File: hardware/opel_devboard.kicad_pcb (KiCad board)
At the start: 2 copper layers, 35 parts, among them P1 CONN_01X16, P2 CONN_01X06, P4 CONN_01X04, P5 CONN_01X04, SW1 SPST, SW2 SPST, U1 ISO1050, U2 LPC11C14, U3 MCP2515_TSSOP, U4 ISO1050, U5 MCP1755

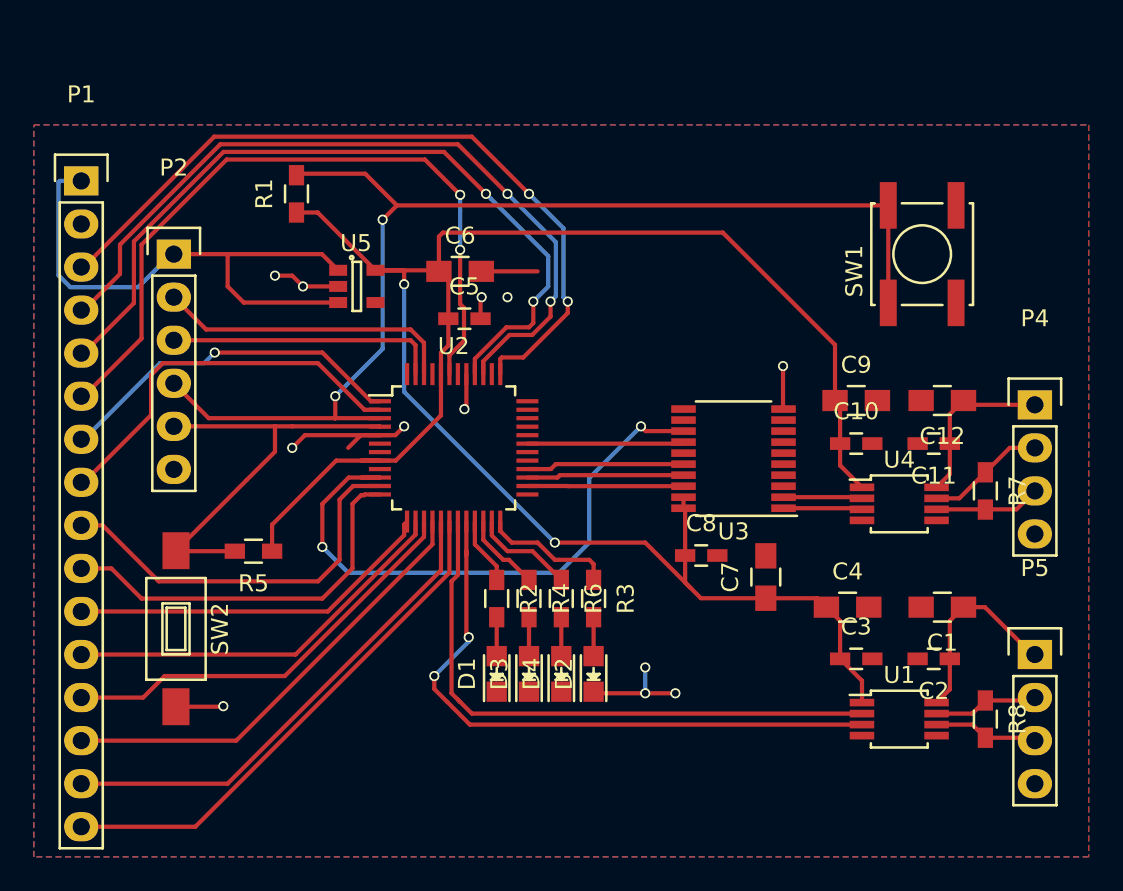
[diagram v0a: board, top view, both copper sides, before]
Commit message: updadted pinout and buttons
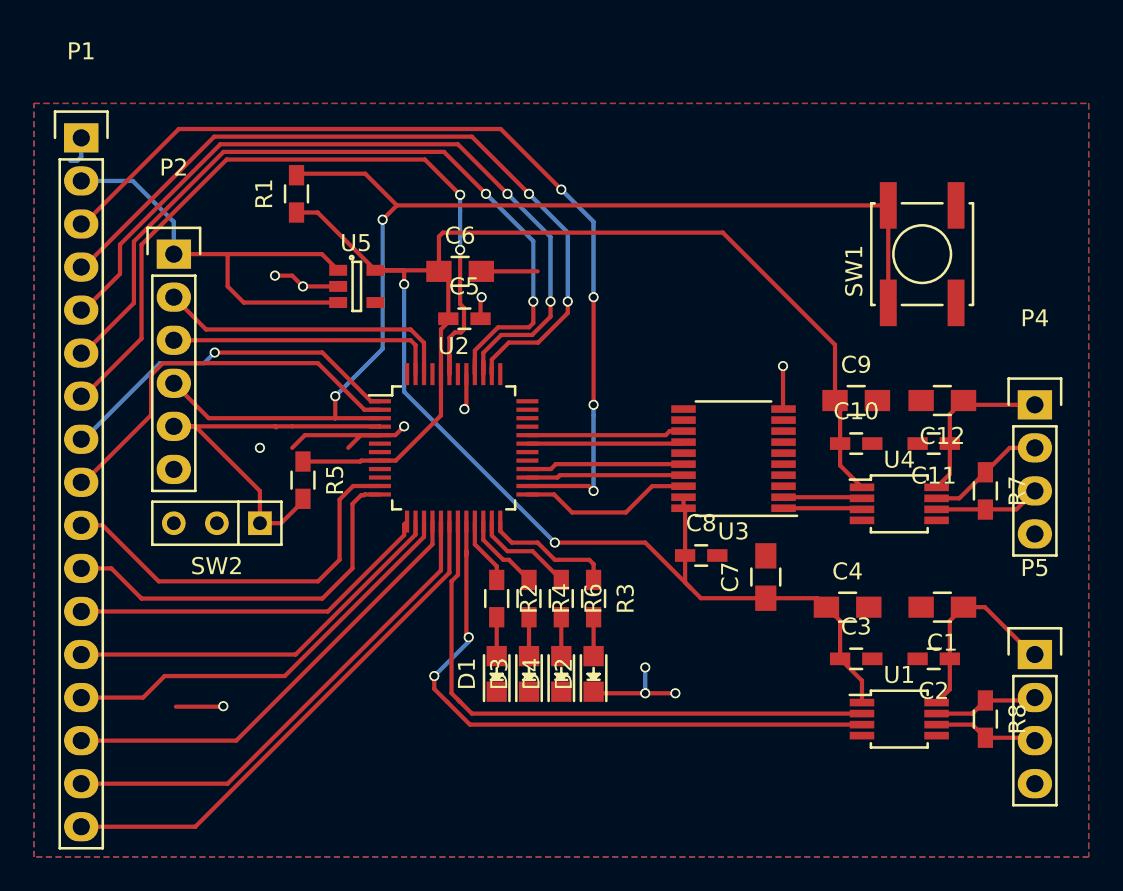
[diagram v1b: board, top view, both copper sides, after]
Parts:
- P1: value CONN_01X16 -> CONN_01X17; footprint Pin_Headers:Pin_Header_Straight_1x16 -> Pin_Headers:Pin_Header_Straight_1x17
- SW2: footprint Buttons_Switches_SMD:SW_SPST_FSMSM -> Buttons_Switches_ThroughHole:SW_Micro_SPST
- moved SW2 6.67 mm to (164.5, 71.8), turned to 180 degrees
- moved R5 5.11 mm to (169.5, 69.2), turned to 270 degrees
- moved P1 2.54 mm to (156.5, 49.0)
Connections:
- P1 pad 1: +5V -> GND
- P1 pad 10: /Micro Controller/PIO2_8 -> /Micro Controller/PIO2_7
- P1 pad 11: /Micro Controller/PIO2_1 -> /Micro Controller/PIO2_8
- P1 pad 12: /Micro Controller/PIO0_3 -> /Micro Controller/PIO2_1
- P1 pad 13: /Micro Controller/PIO0_4 -> /Micro Controller/PIO0_3
- P1 pad 14: /Micro Controller/PIO0_5 -> /Micro Controller/PIO0_4
- P1 pad 15: /Micro Controller/PIO1_9 -> /Micro Controller/PIO0_5
- P1 pad 16: /Micro Controller/PIO2_4 -> /Micro Controller/PIO1_9
- P1 pad 2: GND -> +5V
- P1 pad 3: /Micro Controller/PIO3_1 -> /Micro Controller/PIO2_2
- P1 pad 4: /Micro Controller/PIO1_3 -> /Micro Controller/PIO2_3
- P1 pad 5: /Micro Controller/PIO1_4 -> /Micro Controller/PIO1_3
- P1 pad 6: /Micro Controller/PIO3_2 -> /Micro Controller/PIO1_4
- P1 pad 7: /Micro Controller/PIO2_6 -> /Micro Controller/PIO3_2
- P1 pad 8: /Micro Controller/PIO0_1 -> /Micro Controller/PIO2_6
- P1 pad 9: /Micro Controller/PIO2_7 -> /Micro Controller/PIO0_1
- U2 pad 25: /Micro Controller/PIO2_10 -> Net-(U2-Pad25)
- U2 pad 26: Net-(U2-Pad26) -> /Micro Controller/PIO2_2
- U2 pad 38: Net-(U2-Pad38) -> /Micro Controller/PIO2_3
- U3 pad 13: Net-(U2-Pad10) -> /Micro Controller/PIO0_11
- U3 pad 18: Net-(U2-Pad26) -> Net-(U2-Pad25)
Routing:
- net /Micro Controller/PIO2_2: track 0.00 -> 54.7 mm, vias 0 -> 4
- net /Micro Controller/PIO2_3: track 0.00 -> 45.9 mm, vias 0 -> 2
- net /Micro Controller/PIO3_1: track 45.0 -> 0.00 mm, vias 2 -> 0
- net Net-(U2-Pad10): track 35.5 -> 0.00 mm, vias 2 -> 0
- net Net-(U2-Pad25): track 0.00 -> 10.3 mm
- net /Micro Controller/PIO0_11: track 0.00 -> 9.31 mm
- net Net-(U2-Pad26): track 9.21 -> 0.00 mm
- net +5V: track 33.7 -> 27.4 mm
- net +3V3: track 122.7 -> 116.6 mm
- net (no net): track 0.00 -> 2.81 mm, vias 1 -> 2
- net /Micro Controller/PIO3_2: track 43.3 -> 44.6 mm
- net /Input Connectors/MCU_PROG_N: track 25.4 -> 24.2 mm
- net GND: track 31.8 -> 30.8 mm, vias 11 -> 9
- net /Micro Controller/PIO1_3: track 45.8 -> 46.6 mm

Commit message: panelized
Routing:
- net (no net): track 2.81 -> 0.00 mm, vias 2 -> 1
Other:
- board text added: "+5"
- board text added: "CAN1"
- board text added: "CAN2"
- board text added: "GND"
- board text added: "ISP"
- board text added: "MIT LPC11C DEV"
- board text added: "RESET"
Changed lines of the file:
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@@
   (general
     (links 103)
-    (no_connects 1)
-    (area 0 0 0 0)
+    (no_connects 0)
+    (area 151.355667 42.797 217.833334 91.647001)
     (thickness 1.6)
-    (drawings 0)
-    (tracks 358)
+    (drawings 7)
+    (tracks 355)
     (zones 0)
     (modules 35)
@@
   (layers
     (0 F.Cu signal)
-    (31 B.Cu signal hide)
+    (31 B.Cu signal)
     (32 B.Adhes user)
     (33 F.Adhes user)
@@
     (aux_axis_origin 0 0)
     (grid_origin 212.344 29.845)
-    (visible_elements FFFFFF7F)
+    (visible_elements FFFEFF7F)
     (pcbplotparams
       (layerselection 0x00030_80000001)
@@
     (descr "Through hole pin header")
     (tags "pin header")
-    (fp_text reference P2 (at 0 -5.1) (layer F.SilkS)
+    (fp_text reference P2 (at 0 -2.54) (layer F.SilkS)
       (effects (font (size 1 1) (thickness 0.15)))
     )
@@
     (tags "capacitor 0805")
     (attr smd)
-    (fp_text reference C1 (at 0 -2.1 180) (layer F.SilkS)
+    (fp_text reference C1 (at 0 2.413 180) (layer F.SilkS)
       (effects (font (size 1 1) (thickness 0.15)))
     )
@@
     (tags "capacitor 0603")
     (attr smd)
-    (fp_text reference C2 (at 0 -1.9 180) (layer F.SilkS)
+    (fp_text reference C2 (at -3.048 -0.254 180) (layer F.SilkS)
       (effects (font (size 1 1) (thickness 0.15)))
     )
@@
     (tags "capacitor 0603")
     (attr smd)
-    (fp_text reference C3 (at 0 -1.9) (layer F.SilkS)
+    (fp_text reference C3 (at -3.175 0.254) (layer F.SilkS)
       (effects (font (size 1 1) (thickness 0.15)))
     )
@@
     (tags "capacitor 0805")
     (attr smd)
-    (fp_text reference C4 (at 0 -2.1) (layer F.SilkS)
+    (fp_text reference C4 (at 0 -2.413) (layer F.SilkS)
       (effects (font (size 1 1) (thickness 0.15)))
     )
@@
     (tags "capacitor 0603")
     (attr smd)
-    (fp_text reference C5 (at 0 -1.9) (layer F.SilkS)
+    (fp_text reference C5 (at 3.429 0) (layer F.SilkS)
       (effects (font (size 1 1) (thickness 0.15)))
     )
@@
     (tags "capacitor 0805")
     (attr smd)
-    (fp_text reference C6 (at 0 -2.1) (layer F.SilkS)
+    (fp_text reference C6 (at 3.683 0.254) (layer F.SilkS)
       (effects (font (size 1 1) (thickness 0.15)))
     )
@@
     (tags "capacitor 0805")
     (attr smd)
-    (fp_text reference C7 (at 0 -2.1 90) (layer F.SilkS)
+    (fp_text reference C7 (at -3.175 -0.381 180) (layer F.SilkS)
       (effects (font (size 1 1) (thickness 0.15)))
     )
@@
     (tags "capacitor 0603")
     (attr smd)
-    (fp_text reference C8 (at 0 -1.9) (layer F.SilkS)
+    (fp_text reference C8 (at 0 1.905) (layer F.SilkS)
       (effects (font (size 1 1) (thickness 0.15)))
     )
@@
     (tags "capacitor 0805")
     (attr smd)
-    (fp_text reference C9 (at 0 -2.1) (layer F.SilkS)
+    (fp_text reference C9 (at 0 -1.651) (layer F.SilkS)
       (effects (font (size 1 1) (thickness 0.15)))
     )
@@
     (tags "capacitor 0603")
     (attr smd)
-    (fp_text reference C10 (at 0 -1.9) (layer F.SilkS)
+    (fp_text reference C10 (at -1.905 2.159 90) (layer F.SilkS)
       (effects (font (size 1 1) (thickness 0.15)))
     )
@@
     (tags "capacitor 0603")
     (attr smd)
-    (fp_text reference C11 (at 0 -1.9 180) (layer F.SilkS)
+    (fp_text reference C11 (at -3.048 0.381 180) (layer F.SilkS)
       (effects (font (size 1 1) (thickness 0.15)))
     )
@@
     (tags "capacitor 0805")
     (attr smd)
-    (fp_text reference C12 (at 0 -2.1 180) (layer F.SilkS)
+    (fp_text reference C12 (at 0 1.651 180) (layer F.SilkS)
       (effects (font (size 1 1) (thickness 0.15)))
     )
@@
     (tags "LED 0805 SMD")
     (attr smd)
-    (fp_text reference D1 (at 0 -1.75 90) (layer F.SilkS)
+    (fp_text reference D1 (at 0 -2.921 90) (layer F.SilkS)
       (effects (font (size 1 1) (thickness 0.15)))
     )
@@
     (tags "LED 0805 SMD")
     (attr smd)
-    (fp_text reference D2 (at 0 -1.75 90) (layer F.SilkS)
+    (fp_text reference D2 (at 0 2.794 90) (layer F.SilkS)
       (effects (font (size 1 1) (thickness 0.15)))
     )
@@
     (tags "LED 0805 SMD")
     (attr smd)
-    (fp_text reference D3 (at 0 -1.75 90) (layer F.SilkS)
+    (fp_text reference D3 (at 0 -3.556 90) (layer F.SilkS)
       (effects (font (size 1 1) (thickness 0.15)))
     )
@@
     (tags "LED 0805 SMD")
     (attr smd)
-    (fp_text reference D4 (at 0 -1.75 90) (layer F.SilkS)
+    (fp_text reference D4 (at 0 3.429 90) (layer F.SilkS)
       (effects (font (size 1 1) (thickness 0.15)))
     )
@@
     (descr "Through hole pin header")
     (tags "pin header")
-    (fp_text reference P4 (at 0 -5.1) (layer F.SilkS)
+    (fp_text reference P4 (at 0 -2.54) (layer F.SilkS)
       (effects (font (size 1 1) (thickness 0.15)))
     )
@@
     (descr "Through hole pin header")
     (tags "pin header")
-    (fp_text reference P5 (at 0 -5.1) (layer F.SilkS)
+    (fp_text reference P5 (at 0 -2.667) (layer F.SilkS)
       (effects (font (size 1 1) (thickness 0.15)))
     )
@@
     (tags "resistor 0603")
     (attr smd)
-    (fp_text reference R1 (at 0 -1.9 90) (layer F.SilkS)
+    (fp_text reference R1 (at 3.429 0 180) (layer F.SilkS)
       (effects (font (size 1 1) (thickness 0.15)))
     )
@@
     (tags "resistor 0603")
     (attr smd)
-    (fp_text reference R2 (at 0 -1.9 270) (layer F.SilkS)
+    (fp_text reference R2 (at 0 2.921 270) (layer F.SilkS)
       (effects (font (size 1 1) (thickness 0.15)))
     )
@@
     (tags "resistor 0603")
     (attr smd)
-    (fp_text reference R3 (at 0 -1.9 270) (layer F.SilkS)
+    (fp_text reference R3 (at 0 -2.794 270) (layer F.SilkS)
       (effects (font (size 1 1) (thickness 0.15)))
     )
@@
     (tags "resistor 0603")
     (attr smd)
-    (fp_text reference R4 (at 0 -1.9 270) (layer F.SilkS)
+    (fp_text reference R4 (at 0 3.556 270) (layer F.SilkS)
       (effects (font (size 1 1) (thickness 0.15)))
     )
@@
     (tags "resistor 0603")
     (attr smd)
-    (fp_text reference R5 (at 0 -1.9 270) (layer F.SilkS)
+    (fp_text reference R5 (at -3.175 0.381 360) (layer F.SilkS)
       (effects (font (size 1 1) (thickness 0.15)))
     )
@@
     (tags "resistor 0603")
     (attr smd)
-    (fp_text reference R6 (at 0 -1.9 270) (layer F.SilkS)
+    (fp_text reference R6 (at 0 -3.429 270) (layer F.SilkS)
       (effects (font (size 1 1) (thickness 0.15)))
     )
@@
     (tags "resistor 0603")
     (attr smd)
-    (fp_text reference R7 (at 0 -1.9 270) (layer F.SilkS)
+    (fp_text reference R7 (at 3.175 0 270) (layer F.SilkS)
       (effects (font (size 1 1) (thickness 0.15)))
     )
@@
     (tags "resistor 0603")
     (attr smd)
-    (fp_text reference R8 (at 0 -1.9 270) (layer F.SilkS)
+    (fp_text reference R8 (at 3.683 0 360) (layer F.SilkS)
       (effects (font (size 1 1) (thickness 0.15)))
     )
@@
     (tags "SSOP 0.65")
     (attr smd)
-    (fp_text reference U1 (at 0 -2.6) (layer F.SilkS)
+    (fp_text reference U1 (at 0 3.048) (layer F.SilkS)
       (effects (font (size 1 1) (thickness 0.15)))
     )
@@
     (tags "SSOP 0.65")
     (attr smd)
-    (fp_text reference U3 (at 0 -4.3 180) (layer F.SilkS)
+    (fp_text reference U3 (at 0 4.445 180) (layer F.SilkS)
       (effects (font (size 1 1) (thickness 0.15)))
     )
@@
     (tags "SSOP 0.65")
     (attr smd)
-    (fp_text reference U4 (at 0 -2.6) (layer F.SilkS)
+    (fp_text reference U4 (at 0 2.413) (layer F.SilkS)
       (effects (font (size 1 1) (thickness 0.15)))
     )
@@
     (descr "Through hole pin header")
     (tags "pin header")
-    (fp_text reference P1 (at 0 -5.1) (layer F.SilkS)
+    (fp_text reference P1 (at 3.175 40.513) (layer F.SilkS)
       (effects (font (size 1 1) (thickness 0.15)))
     )
@@
     )
   )
-  (segment (start 162.04968 82.58043) (end 164.81557 82.58043) (width 0.25) (layer F.Cu) (net 0))
-  (segment (start 164.81557 82.58043) (end 164.846 82.55) (width 0.25) (layer F.Cu) (net 0))
-  (via (at 164.846 82.55) (size 0.6) (drill 0.4) (layers F.Cu B.Cu) (net 0))
+  (gr_text "MIT LPC11C DEV\n" (at 186.944 86.36) (layer F.SilkS)
+    (effects (font (size 1.5 1.5) (thickness 0.3)))
+  )
+  (gr_text CAN2 (at 212.344 57.785 270) (layer F.SilkS)
+    (effects (font (size 1.5 1.5) (thickness 0.3)))
+  )
+  (gr_text "CAN1\n" (at 207.264 88.9) (layer F.SilkS)
+    (effects (font (size 1.5 1.5) (thickness 0.3)))
+  )
+  (gr_text ISP (at 164.084 76.835) (layer F.SilkS)
+    (effects (font (size 1.5 1.5) (thickness 0.3)))
+  )
+  (gr_text RESET (at 205.994 49.53) (layer F.SilkS)
+    (effects (font (size 1.5 1.5) (thickness 0.3)))
+  )
+  (gr_text +5 (at 160.909 51.435) (layer F.SilkS)
+    (effects (font (size 1.5 1.5) (thickness 0.3)))
+  )
+  (gr_text GND (at 161.544 48.895) (layer F.SilkS)
+    (effects (font (size 1.5 1.5) (thickness 0.3)))
+  )
   (via (at 167.005 67.31) (size 0.6) (drill 0.4) (layers F.Cu B.Cu) (net 0))
   (segment (start 180.02 59.69) (end 180.02 58.486) (width 0.25) (layer F.Cu) (net 1))

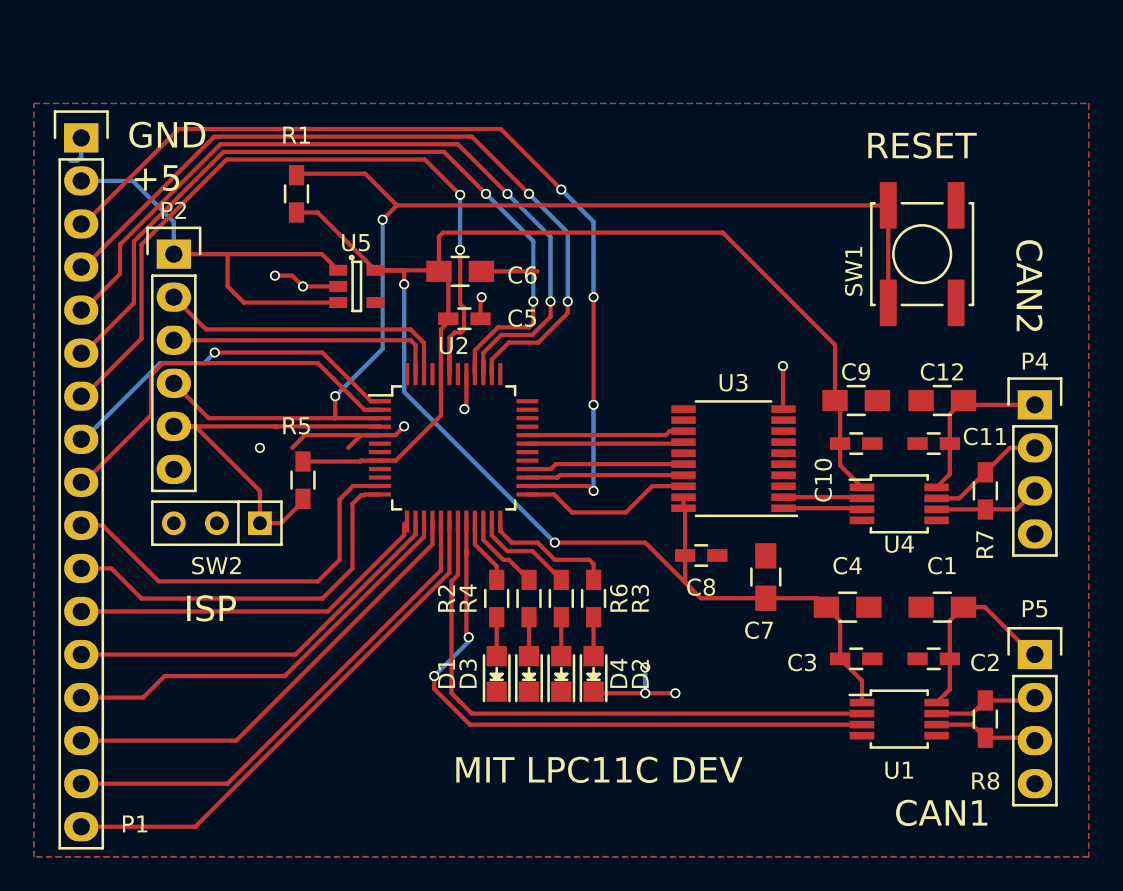
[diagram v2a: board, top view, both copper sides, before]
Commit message: Fixed DRC errors, added labels
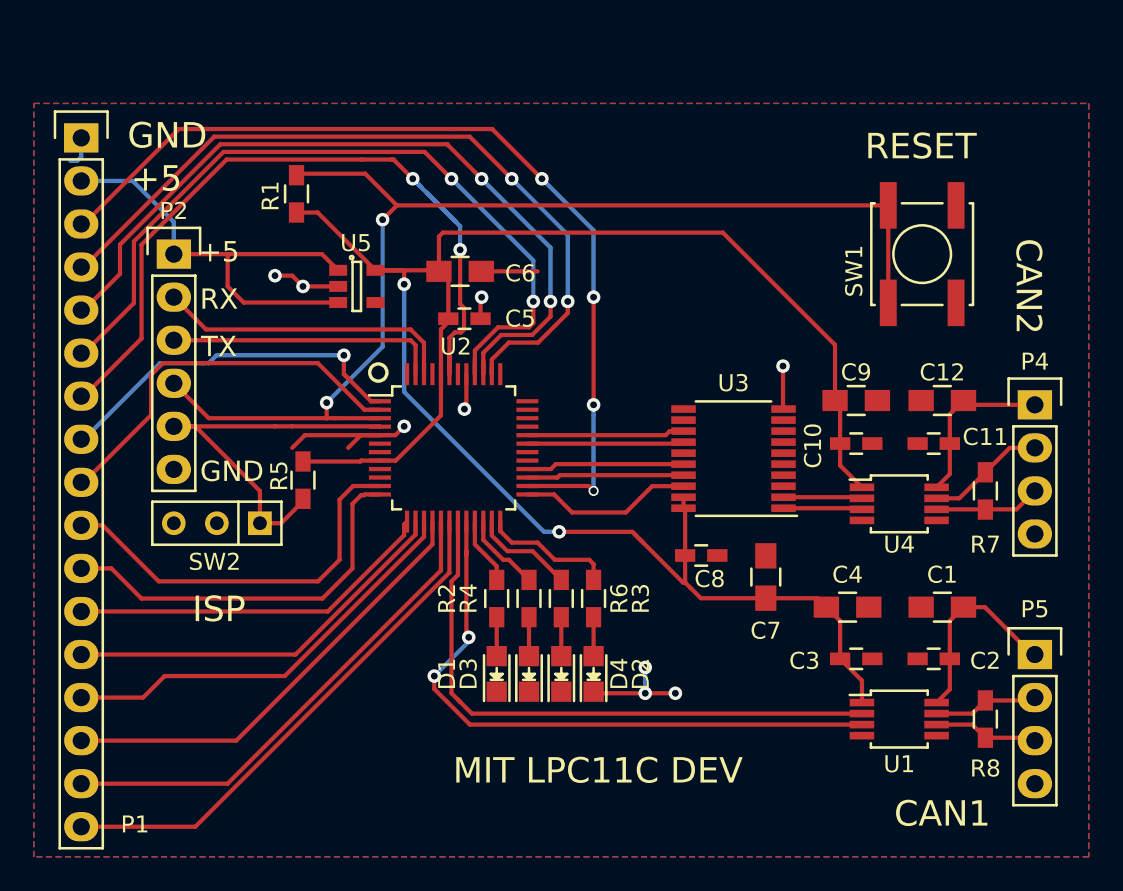
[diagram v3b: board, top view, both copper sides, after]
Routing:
- net /Micro Controller/PIO3_2: track 44.6 -> 46.8 mm
- net /Micro Controller/PIO2_6: track 20.9 -> 22.0 mm
- net /Micro Controller/PIO1_4: track 47.1 -> 46.5 mm
- net (no net): vias 1 -> 0
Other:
- net class Default: via_dia 0.6 -> 0.8
- board text added: "RX"
- board text added: "TX"
